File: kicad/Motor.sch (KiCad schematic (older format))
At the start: 3 parts, among them P1 MT-ENC, U2 DRV8835

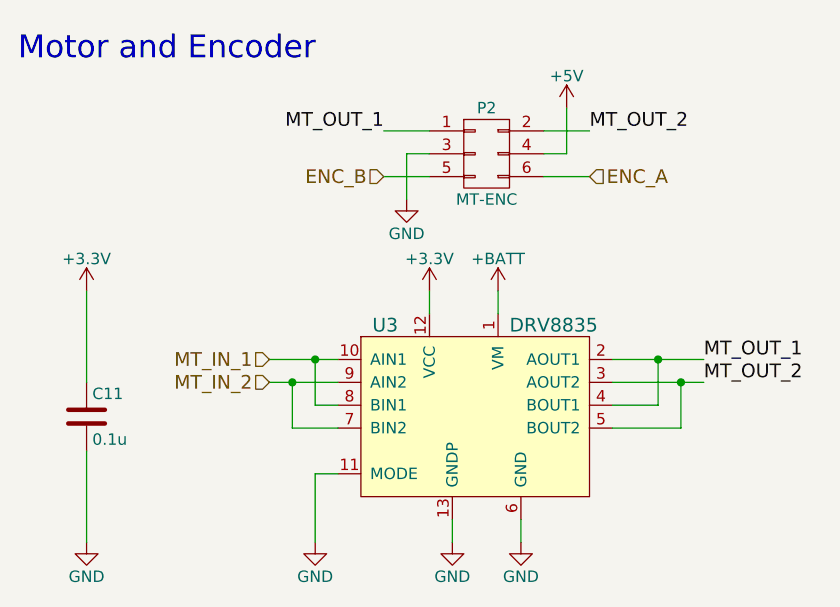
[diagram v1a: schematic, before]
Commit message: 回路図を修正
電源スイッチにPchFETを挿入
赤外線LED用FETのゲートをプルダウン
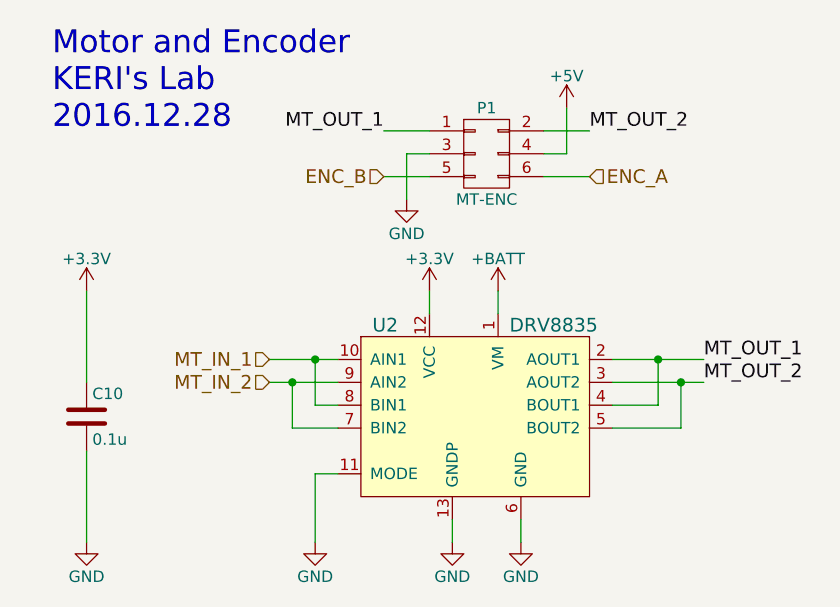
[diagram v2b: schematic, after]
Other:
- note added: "Motor and Encoder\nKERI's Lab\n2016.12.28"
- note removed: "Motor and Encoder"
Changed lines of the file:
@@
 EESchema Schematic File Version 2
+LIBS:KERISEv1-rescue
 LIBS:74xgxx
 LIBS:74xx
@@
 LIBS:cmos4000
 LIBS:conn
-LIBS:connectors
 LIBS:contrib
 LIBS:cypress
@@
 LIBS:ftdi
 LIBS:gennum
-LIBS:graphic
 LIBS:hc11
-LIBS:ic-cpu
-LIBS:ic-io
-LIBS:ic-misc
-LIBS:ic-power
 LIBS:intel
 LIBS:interface
@@
 LIBS:Lattice
 LIBS:linear
-LIBS:logo
 LIBS:maxim
 LIBS:memory
@@
 LIBS:opto
 LIBS:Oscillators
-LIBS:passive
 LIBS:philips
 LIBS:power
@@
 LIBS:Zilog
 LIBS:KERISEv1
-LIBS:kerikun11
 LIBS:KERISEv1-cache
 EELAYER 25 0
@@
 AR Path="/57CA18F6/57CA1E0F" Ref="U2"  Part="1"
 AR Path="/57CA507C/57CA1E0F" Ref="U3"  Part="1"
-F 0 "U3" H 5350 4550 60  0000 L CNN
+F 0 "U2" H 5350 4550 60  0000 L CNN
 F 1 "DRV8835" H 5950 4550 60  0000 L CNN
 F 2 "kerikun11:DRV8835" H 5400 4350 60  0001 C CNN
@@
 Connection ~ 5000 4100
 $Comp
-L +3.3V #PWR11
+L +3.3V #PWR12
 U 1 1 57CA1E2A
 P 5600 3700
-AR Path="/57CA18F6/57CA1E2A" Ref="#PWR11"  Part="1"
-AR Path="/57CA507C/57CA1E2A" Ref="#PWR20"  Part="1"
-F 0 "#PWR20" H 5600 3550 50  0001 C CNN
+AR Path="/57CA18F6/57CA1E2A" Ref="#PWR12"  Part="1"
+AR Path="/57CA507C/57CA1E2A" Ref="#PWR21"  Part="1"
+F 0 "#PWR12" H 5600 3550 50  0001 C CNN
 F 1 "+3.3V" H 5600 3840 50  0000 C CNN
 F 2 "" H 5600 3700 50  0000 C CNN
@@
 	5900 3700 5900 3800
 $Comp
-L GND #PWR15
+L GND #PWR13
 U 1 1 57CA1E38
 P 5700 4800
-AR Path="/57CA18F6/57CA1E38" Ref="#PWR15"  Part="1"
-AR Path="/57CA507C/57CA1E38" Ref="#PWR24"  Part="1"
-F 0 "#PWR24" H 5700 4550 50  0001 C CNN
+AR Path="/57CA18F6/57CA1E38" Ref="#PWR13"  Part="1"
+AR Path="/57CA507C/57CA1E38" Ref="#PWR22"  Part="1"
+F 0 "#PWR13" H 5700 4550 50  0001 C CNN
 F 1 "GND" H 5700 4650 50  0000 C CNN
 F 2 "" H 5700 4800 50  0000 C CNN
@@
 	5700 4800 5700 4700
 $Comp
-L GND #PWR16
+L GND #PWR15
 U 1 1 57CA1E3F
 P 6000 4800
-AR Path="/57CA18F6/57CA1E3F" Ref="#PWR16"  Part="1"
-AR Path="/57CA507C/57CA1E3F" Ref="#PWR25"  Part="1"
-F 0 "#PWR25" H 6000 4550 50  0001 C CNN
+AR Path="/57CA18F6/57CA1E3F" Ref="#PWR15"  Part="1"
+AR Path="/57CA507C/57CA1E3F" Ref="#PWR24"  Part="1"
+F 0 "#PWR15" H 6000 4550 50  0001 C CNN
 F 1 "GND" H 6000 4650 50  0000 C CNN
 F 2 "" H 6000 4800 50  0000 C CNN
@@
 	6000 4800 6000 4700
 $Comp
-L GND #PWR14
+L GND #PWR10
 U 1 1 57CA1E46
 P 5100 4800
-AR Path="/57CA18F6/57CA1E46" Ref="#PWR14"  Part="1"
-AR Path="/57CA507C/57CA1E46" Ref="#PWR23"  Part="1"
-F 0 "#PWR23" H 5100 4550 50  0001 C CNN
+AR Path="/57CA18F6/57CA1E46" Ref="#PWR10"  Part="1"
+AR Path="/57CA507C/57CA1E46" Ref="#PWR19"  Part="1"
+F 0 "#PWR10" H 5100 4550 50  0001 C CNN
 F 1 "GND" H 5100 4650 50  0000 C CNN
 F 2 "" H 5100 4800 50  0000 C CNN
@@
 AR Path="/57CA18F6/57CA1E4E" Ref="P1"  Part="1"
 AR Path="/57CA507C/57CA1E4E" Ref="P2"  Part="1"
-F 0 "P2" H 5850 3300 50  0000 C CNN
+F 0 "P1" H 5850 3300 50  0000 C CNN
 F 1 "MT-ENC" H 5850 2900 50  0000 C CNN
 F 2 "Pin_Headers:Pin_Header_Straight_2x03" H 5850 1900 50  0001 C CNN
@@
 $EndComp
 $Comp
-L GND #PWR9
+L GND #PWR11
 U 1 1 57CA1E57
 P 5500 3300
-AR Path="/57CA18F6/57CA1E57" Ref="#PWR9"  Part="1"
-AR Path="/57CA507C/57CA1E57" Ref="#PWR18"  Part="1"
-F 0 "#PWR18" H 5500 3050 50  0001 C CNN
+AR Path="/57CA18F6/57CA1E57" Ref="#PWR11"  Part="1"
+AR Path="/57CA507C/57CA1E57" Ref="#PWR20"  Part="1"
+F 0 "#PWR11" H 5500 3050 50  0001 C CNN
 F 1 "GND" H 5500 3150 50  0000 C CNN
 F 2 "" H 5500 3300 50  0000 C CNN
@@
 	6300 3200 6100 3200
 $Comp
-L +5V #PWR8
+L +5V #PWR16
 U 1 1 57CA1E65
 P 6200 2900
-AR Path="/57CA18F6/57CA1E65" Ref="#PWR8"  Part="1"
-AR Path="/57CA507C/57CA1E65" Ref="#PWR17"  Part="1"
-F 0 "#PWR17" H 6200 2750 50  0001 C CNN
+AR Path="/57CA18F6/57CA1E65" Ref="#PWR16"  Part="1"
+AR Path="/57CA507C/57CA1E65" Ref="#PWR25"  Part="1"
+F 0 "#PWR16" H 6200 2750 50  0001 C CNN
 F 1 "+5V" H 6200 3040 50  0000 C CNN
 F 2 "" H 6200 2900 50  0000 C CNN
@@
 Text HLabel 4900 4100 0    60   Input ~ 0
 MT_IN_2
-Text Notes 3800 2700 0    100  ~ 0
-Motor and Encoder
+Text Notes 3950 3000 0    100  ~ 0
+Motor and Encoder\nKERI's Lab\n2016.12.28
 $Comp
 L C C10
@@
 AR Path="/57CA18F6/57CCEFE0" Ref="C10"  Part="1"
 AR Path="/57CA507C/57CCEFE0" Ref="C11"  Part="1"
-F 0 "C11" H 4125 4350 50  0000 L CNN
+F 0 "C10" H 4125 4350 50  0000 L CNN
 F 1 "0.1u" H 4125 4150 50  0000 L CNN
 F 2 "Capacitors_SMD:C_0603" H 4138 4100 50  0001 C CNN
@@
 $EndComp
 $Comp
-L +3.3V #PWR10
+L +3.3V #PWR8
 U 1 1 57CCF032
 P 4100 3700
-AR Path="/57CA18F6/57CCF032" Ref="#PWR10"  Part="1"
-AR Path="/57CA507C/57CCF032" Ref="#PWR19"  Part="1"
-F 0 "#PWR19" H 4100 3550 50  0001 C CNN
+AR Path="/57CA18F6/57CCF032" Ref="#PWR8"  Part="1"
+AR Path="/57CA507C/57CCF032" Ref="#PWR17"  Part="1"
+F 0 "#PWR8" H 4100 3550 50  0001 C CNN
 F 1 "+3.3V" H 4100 3840 50  0000 C CNN
 F 2 "" H 4100 3700 50  0000 C CNN
@@
 $EndComp
 $Comp
-L GND #PWR13
+L GND #PWR9
 U 1 1 57CCF046
 P 4100 4800
-AR Path="/57CA18F6/57CCF046" Ref="#PWR13"  Part="1"
-AR Path="/57CA507C/57CCF046" Ref="#PWR22"  Part="1"
-F 0 "#PWR22" H 4100 4550 50  0001 C CNN
+AR Path="/57CA18F6/57CCF046" Ref="#PWR9"  Part="1"
+AR Path="/57CA507C/57CCF046" Ref="#PWR18"  Part="1"
+F 0 "#PWR9" H 4100 4550 50  0001 C CNN
 F 1 "GND" H 4100 4650 50  0000 C CNN
 F 2 "" H 4100 4800 50  0000 C CNN
@@
 	4100 4400 4100 4800
 $Comp
-L +BATT #PWR12
+L +BATT #PWR14
 U 1 1 57CD5BEE
 P 5900 3700
-AR Path="/57CA18F6/57CD5BEE" Ref="#PWR12"  Part="1"
-AR Path="/57CA507C/57CD5BEE" Ref="#PWR21"  Part="1"
-F 0 "#PWR21" H 5900 3550 50  0001 C CNN
+AR Path="/57CA18F6/57CD5BEE" Ref="#PWR14"  Part="1"
+AR Path="/57CA507C/57CD5BEE" Ref="#PWR23"  Part="1"
+F 0 "#PWR14" H 5900 3550 50  0001 C CNN
 F 1 "+BATT" H 5900 3840 50  0000 C CNN
 F 2 "" H 5900 3700 50  0000 C CNN

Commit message: add kicad .gitignore
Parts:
- C10: symbol C -> KERISEv1-rescue:C
- P1: symbol CONN_02X03 -> KERISEv1-rescue:CONN_02X03
- U2: symbol DRV8835 -> KERISEv1:DRV8835
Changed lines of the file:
@@
-EESchema Schematic File Version 2
-LIBS:KERISEv1-rescue
-LIBS:74xgxx
-LIBS:74xx
-LIBS:ac-dc
-LIBS:actel
-LIBS:adc-dac
-LIBS:Altera
-LIBS:analog_devices
-LIBS:analog_switches
-LIBS:atmel
-LIBS:audio
-LIBS:brooktre
-LIBS:cmos_ieee
-LIBS:cmos4000
-LIBS:conn
-LIBS:contrib
-LIBS:cypress
-LIBS:dc-dc
-LIBS:device
-LIBS:digital-audio
-LIBS:diode
-LIBS:display
-LIBS:dsp
-LIBS:elec-unifil
-LIBS:ESD_Protection
-LIBS:ftdi
-LIBS:gennum
-LIBS:hc11
-LIBS:intel
-LIBS:interface
-LIBS:ir
-LIBS:Lattice
-LIBS:linear
-LIBS:maxim
-LIBS:memory
-LIBS:microchip
-LIBS:microchip_dspic33dsc
-LIBS:microchip_pic10mcu
-LIBS:microchip_pic12mcu
-LIBS:microchip_pic16mcu
-LIBS:microchip_pic18mcu
-LIBS:microchip_pic32mcu
-LIBS:microcontrollers
-LIBS:motor_drivers
-LIBS:motorola
-LIBS:msp430
-LIBS:nordicsemi
-LIBS:nxp_armmcu
-LIBS:onsemi
-LIBS:opto
-LIBS:Oscillators
-LIBS:philips
-LIBS:power
-LIBS:Power_Management
-LIBS:powerint
-LIBS:pspice
-LIBS:references
-LIBS:regul
-LIBS:relays
-LIBS:rfcom
-LIBS:sensors
-LIBS:silabs
-LIBS:siliconi
-LIBS:stm8
-LIBS:stm32
-LIBS:supertex
-LIBS:switches
-LIBS:texas
-LIBS:transf
-LIBS:transistors
-LIBS:ttl_ieee
-LIBS:valves
-LIBS:video
-LIBS:Xicor
-LIBS:xilinx
-LIBS:Zilog
-LIBS:KERISEv1
-LIBS:KERISEv1-cache
-EELAYER 25 0
+EESchema Schematic File Version 4
+EELAYER 30 0
 EELAYER END
 $Descr A4 11693 8268
@@
 $EndDescr
 $Comp
-L DRV8835 U2
+L KERISEv1:DRV8835 U2
 U 1 1 57CA1E0F
 P 5800 4200
@@
 Connection ~ 5000 4100
 $Comp
-L +3.3V #PWR12
+L power:+3.3V #PWR12
 U 1 1 57CA1E2A
 P 5600 3700
@@
 	5900 3700 5900 3800
 $Comp
-L GND #PWR13
+L power:GND #PWR13
 U 1 1 57CA1E38
 P 5700 4800
@@
 	5700 4800 5700 4700
 $Comp
-L GND #PWR15
+L power:GND #PWR15
 U 1 1 57CA1E3F
 P 6000 4800
@@
 	6000 4800 6000 4700
 $Comp
-L GND #PWR10
+L power:GND #PWR10
 U 1 1 57CA1E46
 P 5100 4800
@@
 	5100 4500 5200 4500
 $Comp
-L CONN_02X03 P1
+L KERISEv1-rescue:CONN_02X03 P1
 U 1 1 57CA1E4E
 P 5850 3100
 AR Path="/57CA18F6/57CA1E4E" Ref="P1"  Part="1"
 AR Path="/57CA507C/57CA1E4E" Ref="P2"  Part="1"
+AR Path="/57CA1E4E" Ref="P1"  Part="1"
 F 0 "P1" H 5850 3300 50  0000 C CNN
 F 1 "MT-ENC" H 5850 2900 50  0000 C CNN
@@
 $EndComp
 $Comp
-L GND #PWR11
+L power:GND #PWR11
 U 1 1 57CA1E57
 P 5500 3300
@@
 	6300 3200 6100 3200
 $Comp
-L +5V #PWR16
+L power:+5V #PWR16
 U 1 1 57CA1E65
 P 6200 2900
@@
 Motor and Encoder\nKERI's Lab\n2016.12.28
 $Comp
-L C C10
+L KERISEv1-rescue:C C10
 U 1 1 57CCEFE0
 P 4100 4250
 AR Path="/57CA18F6/57CCEFE0" Ref="C10"  Part="1"
 AR Path="/57CA507C/57CCEFE0" Ref="C11"  Part="1"
+AR Path="/57CCEFE0" Ref="C10"  Part="1"
 F 0 "C10" H 4125 4350 50  0000 L CNN
 F 1 "0.1u" H 4125 4150 50  0000 L CNN
@@
 $EndComp
 $Comp
-L +3.3V #PWR8
+L power:+3.3V #PWR8
 U 1 1 57CCF032
 P 4100 3700
@@
 $EndComp
 $Comp
-L GND #PWR9
+L power:GND #PWR9
 U 1 1 57CCF046
 P 4100 4800
@@
 	4100 4400 4100 4800
 $Comp
-L +BATT #PWR14
+L power:+BATT #PWR14
 U 1 1 57CD5BEE
 P 5900 3700
